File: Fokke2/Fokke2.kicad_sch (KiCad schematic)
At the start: 28 parts

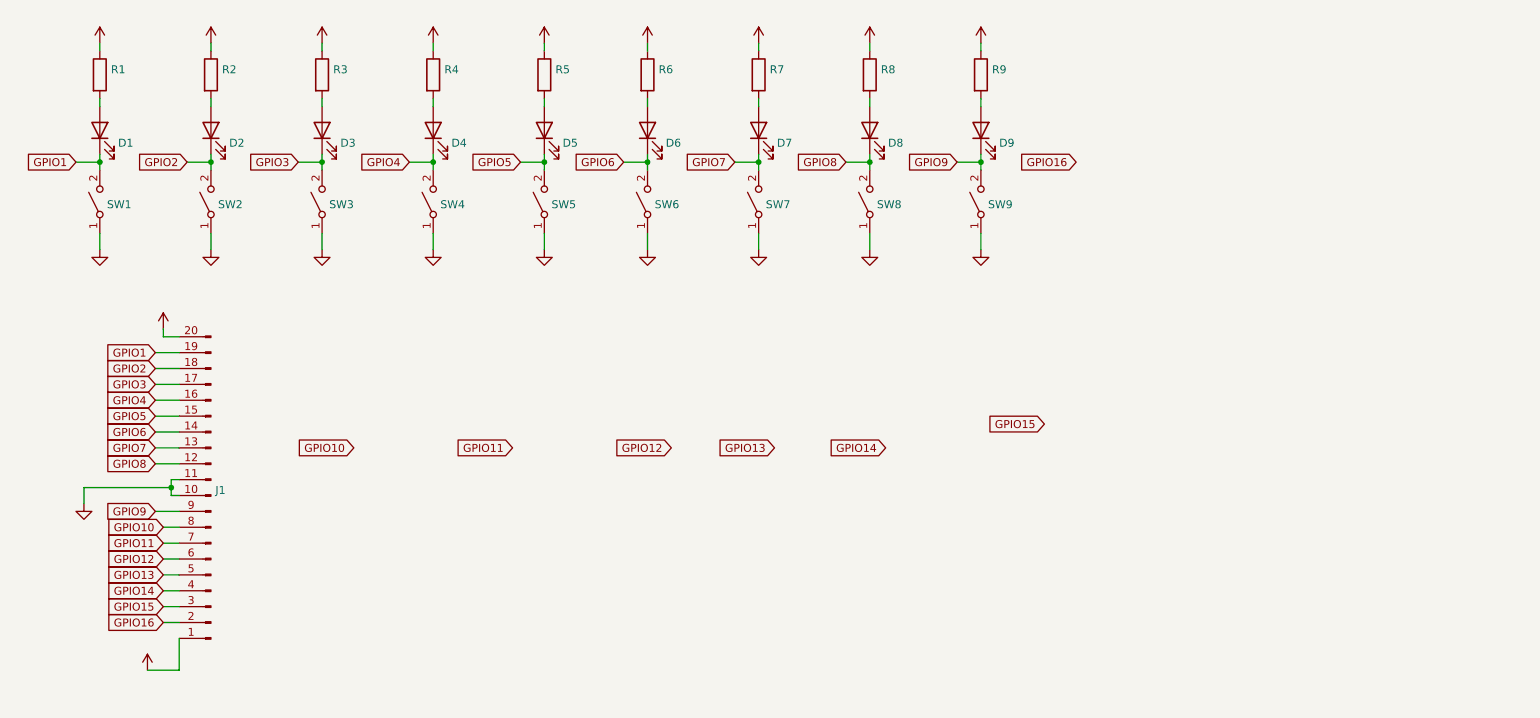
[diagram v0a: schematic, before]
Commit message: did alot of work on Fokke2. The connector is still needed. Also going to make a module flatcable controller line
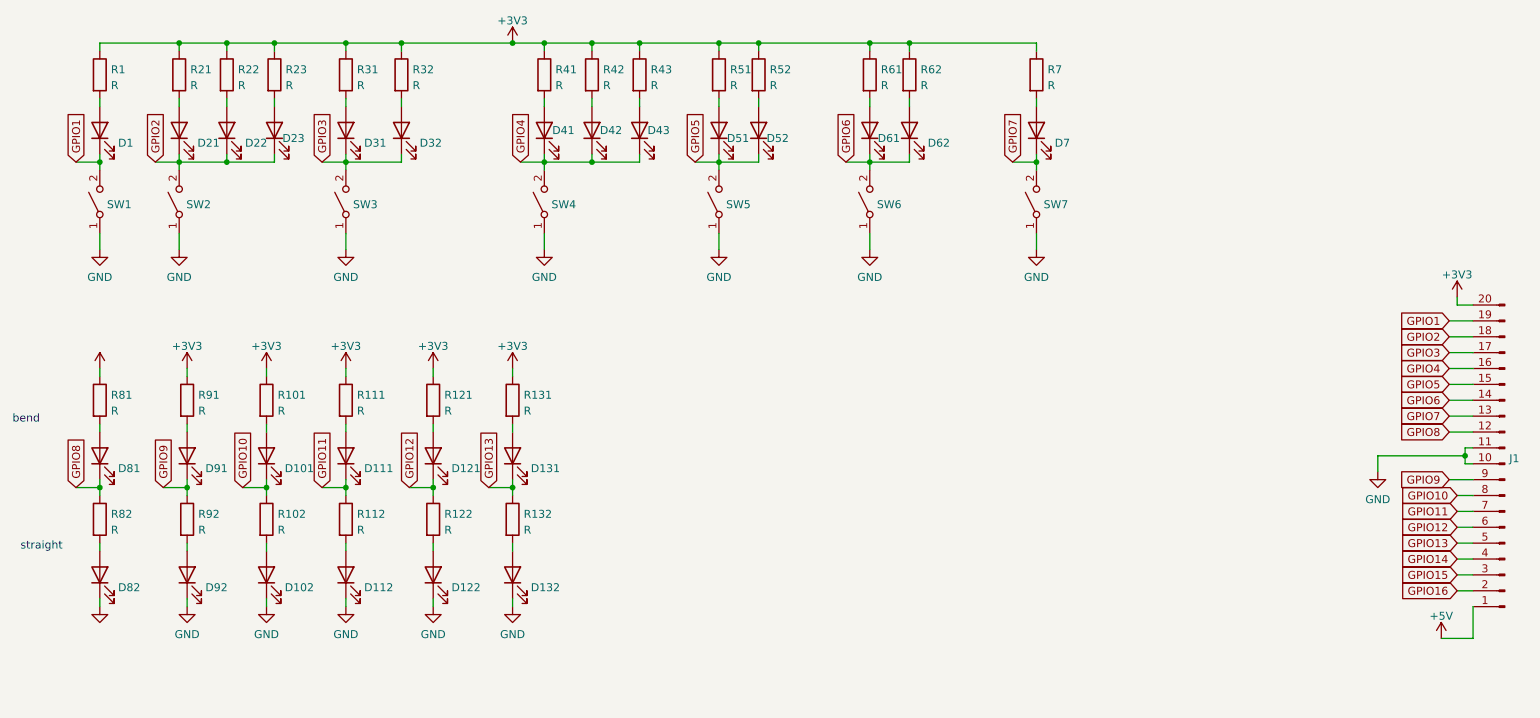
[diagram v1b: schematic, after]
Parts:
- removed D4, D8, D9: (no value), symbol Device:LED
- removed R4, R8, R9: (no value), symbol Device:R
- removed SW8, SW9: (no value), symbol Switch:SW_SPST
- added D101, D102, D111, D112, D121, D122, D131, D132, D22, D23, D32, D41, D42, D43, D52, D62, D81, D82, D91, D92: LED, LED_THT:LED_D3.0mm, symbol Device:LED
- added R101, R102, R111, R112, R121, R122, R131, R132, R22, R23, R32, R41, R42, R43, R52, R62, R81, R82, R91, R92: R, Resistor_SMD:R_0805_2012Metric_Pad1.20x1.40mm_HandSolder, symbol Device:R
- D1, D7: value (none) -> LED; footprint (none) -> LED_THT:LED_D3.0mm
- D21: renamed from D2; value (none) -> LED; footprint (none) -> LED_THT:LED_D3.0mm
- D31: renamed from D3; value (none) -> LED; footprint (none) -> LED_THT:LED_D3.0mm
- D51: renamed from D5; value (none) -> LED; footprint (none) -> LED_THT:LED_D3.0mm
- D61: renamed from D6; value (none) -> LED; footprint (none) -> LED_THT:LED_D3.0mm
- J1: value (none) -> Conn_01x20_Male; footprint (none) -> Connector_PinHeader_2.54mm:PinHeader_1x20_P2.54mm_Vertical
- R1, R7: value (none) -> R; footprint (none) -> Resistor_SMD:R_0805_2012Metric_Pad1.20x1.40mm_HandSolder
- R21: renamed from R2; value (none) -> R; footprint (none) -> Resistor_SMD:R_0805_2012Metric_Pad1.20x1.40mm_HandSolder
- R31: renamed from R3; value (none) -> R; footprint (none) -> Resistor_SMD:R_0805_2012Metric_Pad1.20x1.40mm_HandSolder
- R51: renamed from R5; value (none) -> R; footprint (none) -> Resistor_SMD:R_0805_2012Metric_Pad1.20x1.40mm_HandSolder
- R61: renamed from R6; value (none) -> R; footprint (none) -> Resistor_SMD:R_0805_2012Metric_Pad1.20x1.40mm_HandSolder
- SW1, SW2, SW3, SW4, SW5, SW6, SW7: value (none) -> SW_SPST; footprint (none) -> Button_Switch_THT:SW_PUSH_6mm_H4.3mm
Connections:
- net +3V3: now also R1.1, R21.1, R31.1, R51.1, R61.1, R7.1, R101.1, R111.1, R121.1, R131.1, R22.1, R23.1, R32.1, R41.1, R42.1, R43.1, R52.1, R62.1, R81.1, R91.1
- net +5V: no longer R1.1, R21.1, R31.1, R51.1, R61.1, R7.1
- net GND: now also D102.1 (K), D112.1 (K), D122.1 (K), D132.1 (K), D82.1 (K), D92.1 (K)
- net GPIO10: now also D101.1 (K), R102.1
- net GPIO11: now also D111.1 (K), R112.1
- net GPIO12: now also D121.1 (K), R122.1
- net GPIO13: now also D131.1 (K), R132.1
- net GPIO2: now also D22.1 (K), D23.1 (K)
- net GPIO3: now also D32.1 (K)
- net GPIO4: now also D41.1 (K), D42.1 (K), D43.1 (K)
- net GPIO5: now also D52.1 (K)
- net GPIO6: now also D62.1 (K)
- net GPIO8: now also D81.1 (K), R82.1
- net GPIO9: now also D91.1 (K), R92.1
- new net: D91.2 (A), R91.2
- new net: D42.2 (A), R42.2
- new net: D43.2 (A), R43.2
- new net: D81.2 (A), R81.2
- new net: D131.2 (A), R131.2
- new net: D52.2 (A), R52.2
- new net: D23.2 (A), R23.2
- new net: D132.2 (A), R132.2
- new net: D122.2 (A), R122.2
- new net: D121.2 (A), R121.2
- new net: D82.2 (A), R82.2
- new net: D41.2 (A), R41.2
- new net: D101.2 (A), R101.2
- new net: D111.2 (A), R111.2
- new net: D112.2 (A), R112.2
- new net: D32.2 (A), R32.2
- new net: D22.2 (A), R22.2
- new net: D102.2 (A), R102.2
- new net: D62.2 (A), R62.2
- new net: D92.2 (A), R92.2
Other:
- note added: "bend"
- note added: "straight"
- moved on the sheet: D21, D31, D51, D61, D7, J1, R21, R31, R51, R61, R7, SW2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

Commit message: I added a button to Fokke 1 for his gate, but I lost annonation with the schematic. The schematic as is now is FUBAR. The project however is finished so I got lucky...
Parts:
- removed J1: Conn_01x20_Male, Connector_PinHeader_2.54mm:PinHeader_1x20_P2.54mm_Vertical, symbol Connector:Conn_01x20_Male
- added J101: (no value), symbol Connector:6P6C
- added J102: (no value), symbol custom_kicad_lib_sk:panelX_controller
- R41: value R -> (none); footprint Resistor_SMD:R_0805_2012Metric_Pad1.20x1.40mm_HandSolder -> (none)
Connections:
- net +3V3: now also J102.1 (3V3)
- net +5V: now also J102.2 (5V)
- net GND: now also J101.2, J102.10 (GND)
- net GPIO1: now also J102.23 (GPIO1)
- net GPIO10: now also D21.1 (K), D22.1 (K), D23.1 (K), SW2.2 (B), J102.13 (GPIO10); no longer D101.1 (K), R102.1
- net GPIO11: now also D121.1 (K), R122.1, J102.11 (GPIO11); no longer D111.1 (K), R112.1
- net GPIO12: now also D131.1 (K), R132.1, J102.9 (GPIO12); no longer D121.1 (K), R122.1
- net GPIO13: now also D7.1 (K), SW7.2 (B), J102.7 (GPIO13); no longer D131.1 (K), R132.1
- net GPIO2: now also D81.1 (K), R82.1, J102.24 (GPIO2); no longer D21.1 (K), D22.1 (K), D23.1 (K), SW2.2 (B)
- net GPIO3: now also D101.1 (K), R102.1, J102.21 (GPIO3); no longer D31.1 (K), D32.1 (K), SW3.2 (B)
- net GPIO4: now also D91.1 (K), R92.1, J102.22 (GPIO4); no longer D41.1 (K), D42.1 (K), D43.1 (K), SW4.2 (B)
- net GPIO5: now also D41.1 (K), D42.1 (K), D43.1 (K), SW4.2 (B), J102.19 (GPIO5); no longer D51.1 (K), D52.1 (K), SW5.2 (B)
- net GPIO6: now also D111.1 (K), R112.1, J102.20 (GPIO6); no longer D61.1 (K), D62.1 (K), SW6.2 (B)
- net GPIO7: now also D51.1 (K), D52.1 (K), SW5.2 (B), J102.17 (GPIO7); no longer D7.1 (K), SW7.2 (B)
- net GPIO8: now also D61.1 (K), D62.1 (K), SW6.2 (B), J102.18 (GPIO8); no longer D81.1 (K), R82.1
- net GPIO9: now also D31.1 (K), D32.1 (K), SW3.2 (B), J102.15 (GPIO9); no longer D91.1 (K), R92.1
- new net: J101.3, J102.8 (B)
- new net: J101.4, J102.6 (A)
- new net +12V: J101.5, J102.4 (12V)
- no-connect marks 0 -> 7
